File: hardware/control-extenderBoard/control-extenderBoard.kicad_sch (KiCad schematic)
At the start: 149 parts, among them J1 12V + GND (TP), J10 SCL6 + GND (TP), J11 SDA6 + GND (TP), J12 3V3 + GND (TP), J13 12V + GND (TP), J14 SCL6 + GND (TP), J15 SDA6 + GND (TP), J17 24V IN, J18 GND, J22 SDA, SCL - ESP32, J23 I2C Reserve SCL/GND, J24 I2C Reserve SDA/GND, J25 I2C Reserve SDA/GND, J26 I2C Reserve SCL/GND, J27 CAT6-Shield, J28 CAT6-Shield, J29 Chassis, J3 Conn_01x02_Pin, J30 RX TX, J31 DIR, GND, J32 12V out, J33 5V out, J34 3V3 out, J35 Conn_01x02_Pin, J36 Conn_01x02_Pin, J37 Conn_01x02_Pin, J38 Conn_01x02_Pin, J39 Conn_01x02_Pin, J4 3V3 + GND (TP), J5 GND, J6 SCL7 Differential (TP), J7 SDA7 Differential (TP), J8 RS485, J9 Conn_01x03_Pin, U1 MAX3485, U10 LM2576T-12, U2 PCA9600D, U3 TCA9548A_1-to-8_I2C_Multiplex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, U4 LM2576T-3.3, U5 PCA9600D, U6 PCA82C251, U7 PCA82C251, U8 PCA9600D, U9 LM2576T-5

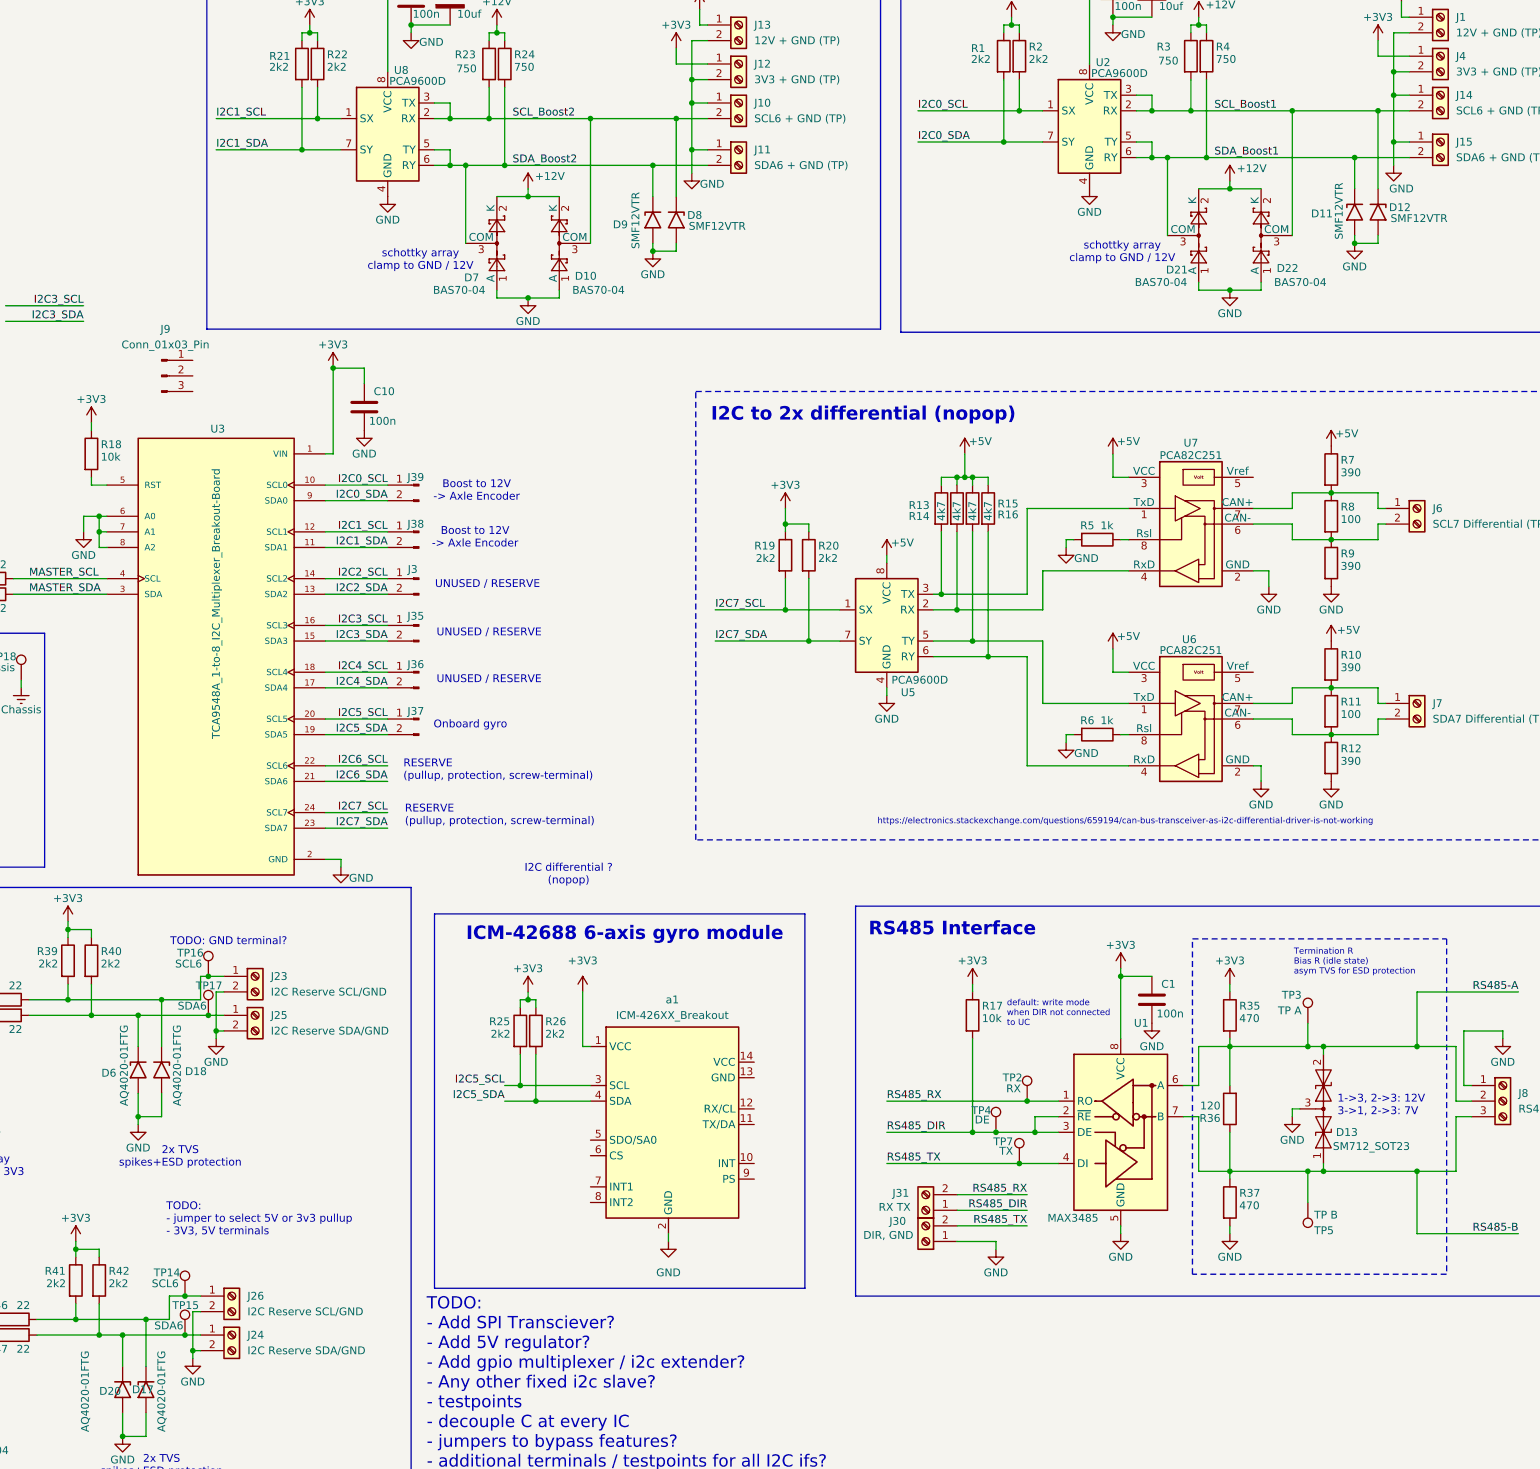
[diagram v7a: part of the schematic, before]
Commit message: extenderBoard: Add pcb text, Arrange remote-board
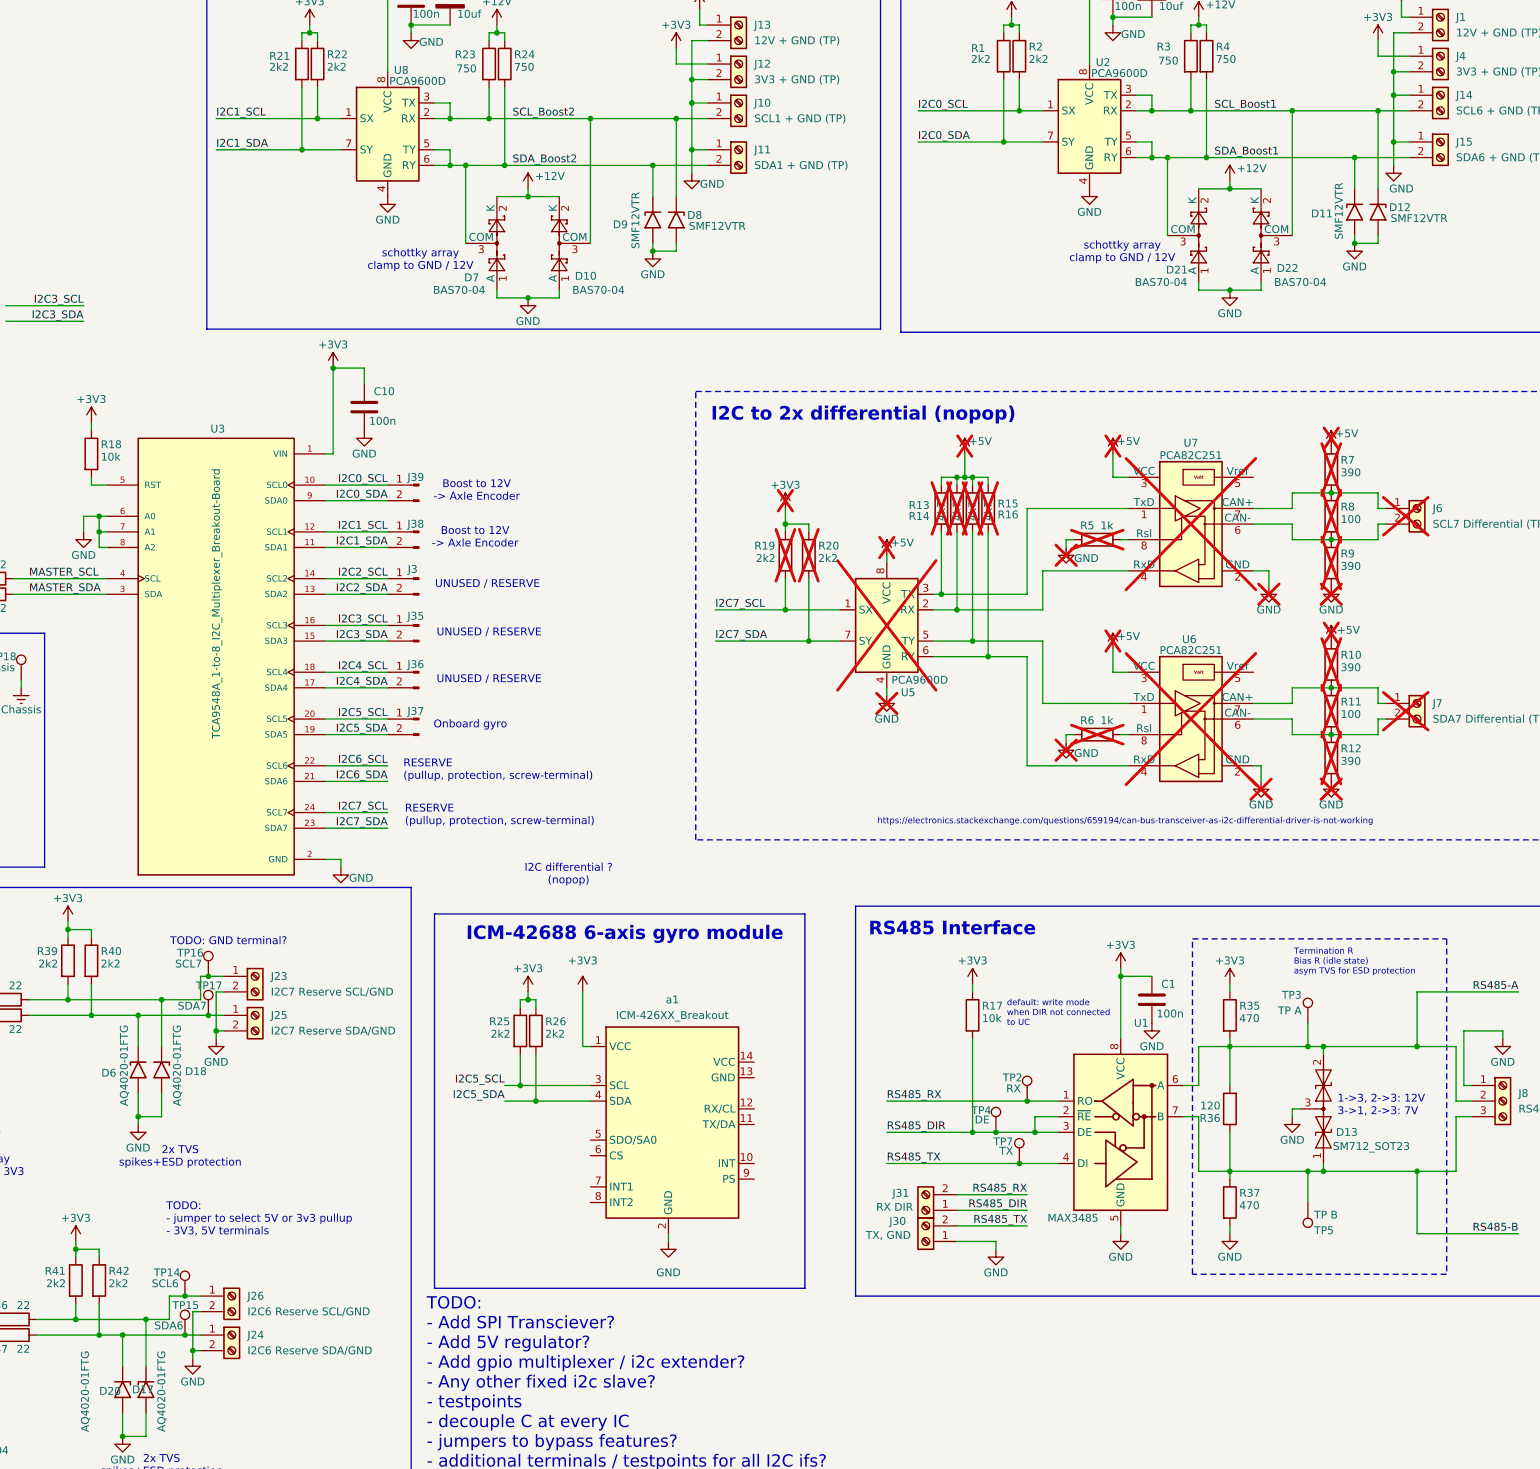
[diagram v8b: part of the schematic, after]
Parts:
- removed J9: Conn_01x03_Pin, Connector_PinHeader_2.54mm:PinHeader_1x03_P2.54mm_Vertical, symbol Connector:Conn_01x03_Pin
- J10: value SCL6 + GND (TP) -> SCL1 + GND (TP)
- J11: value SDA6 + GND (TP) -> SDA1 + GND (TP)
- J23: value I2C Reserve SCL/GND -> I2C7 Reserve SCL/GND
- J24: value I2C Reserve SDA/GND -> I2C6 Reserve SDA/GND
- J25: value I2C Reserve SDA/GND -> I2C7 Reserve SDA/GND
- J26: value I2C Reserve SCL/GND -> I2C6 Reserve SCL/GND
- J30: value RX TX -> RX DIR
- J31: value DIR, GND -> TX, GND
- J6, J7, R10, R11, R12, R13, R14, R15, R16, R19, R20, R5, R6, R7, R8, R9, U5, U6, U7: now not fitted; now left out of the parts list
- TP16: value SCL6 -> SCL7
- TP17: value SDA6 -> SDA7
